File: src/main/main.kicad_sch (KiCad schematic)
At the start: 14 parts, among them J101 Conn_02x05_Odd_Even, P101 SMTSO3035CTJ, P102 SMTSO3035CTJ, P103 SMTSO3035CTJ, P104 SMTSO3035CTJ, U101 LTV-817S

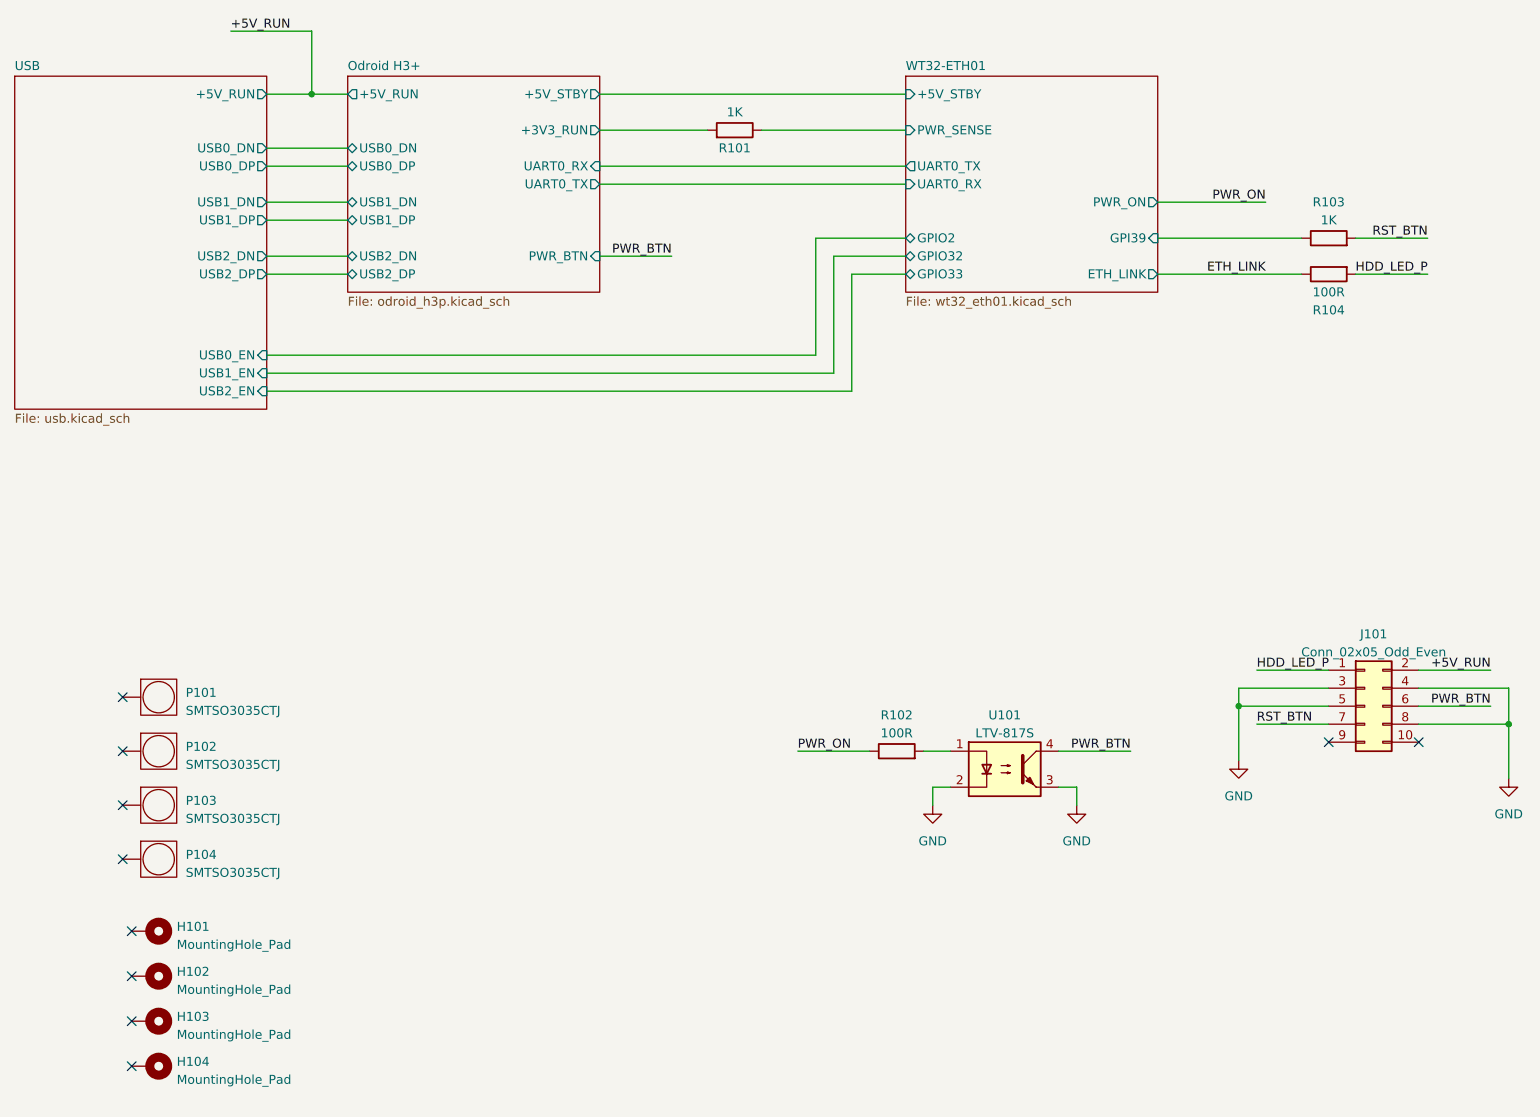
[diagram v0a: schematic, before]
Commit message: Additions and fixes:
Add:
- Add power rail LED status indicators
- Buffered LED on ETH_LINK
- GPIO14 and GPIO12 on header
- GPIO14 5V buffered output on header
- Testpoints for GPIO0 and ESP32_ENABLE pin
- Reset and Boot switches
- ESP PWR selector switch
- USB Type-C PD input (5V) for ESP32
- 1.1A Fuse for USB PD input
- Add spot for BIOS battery on silk
- Add silkscreen default jumper marking
- Add GPIO39 external pullup to 3V3
- Add pulldown to PWR_BUTTON (GPIO15)
- Add silkscreen github link

Fixes:
- Clarify things on silk
- Make pinout compatible with USB-UART boards
  - Move GPI0 and ENABLE to testpoints
- Silkscreen alignment fixes

Removed:
- 3 APA102 LEDs
- Remove JP201
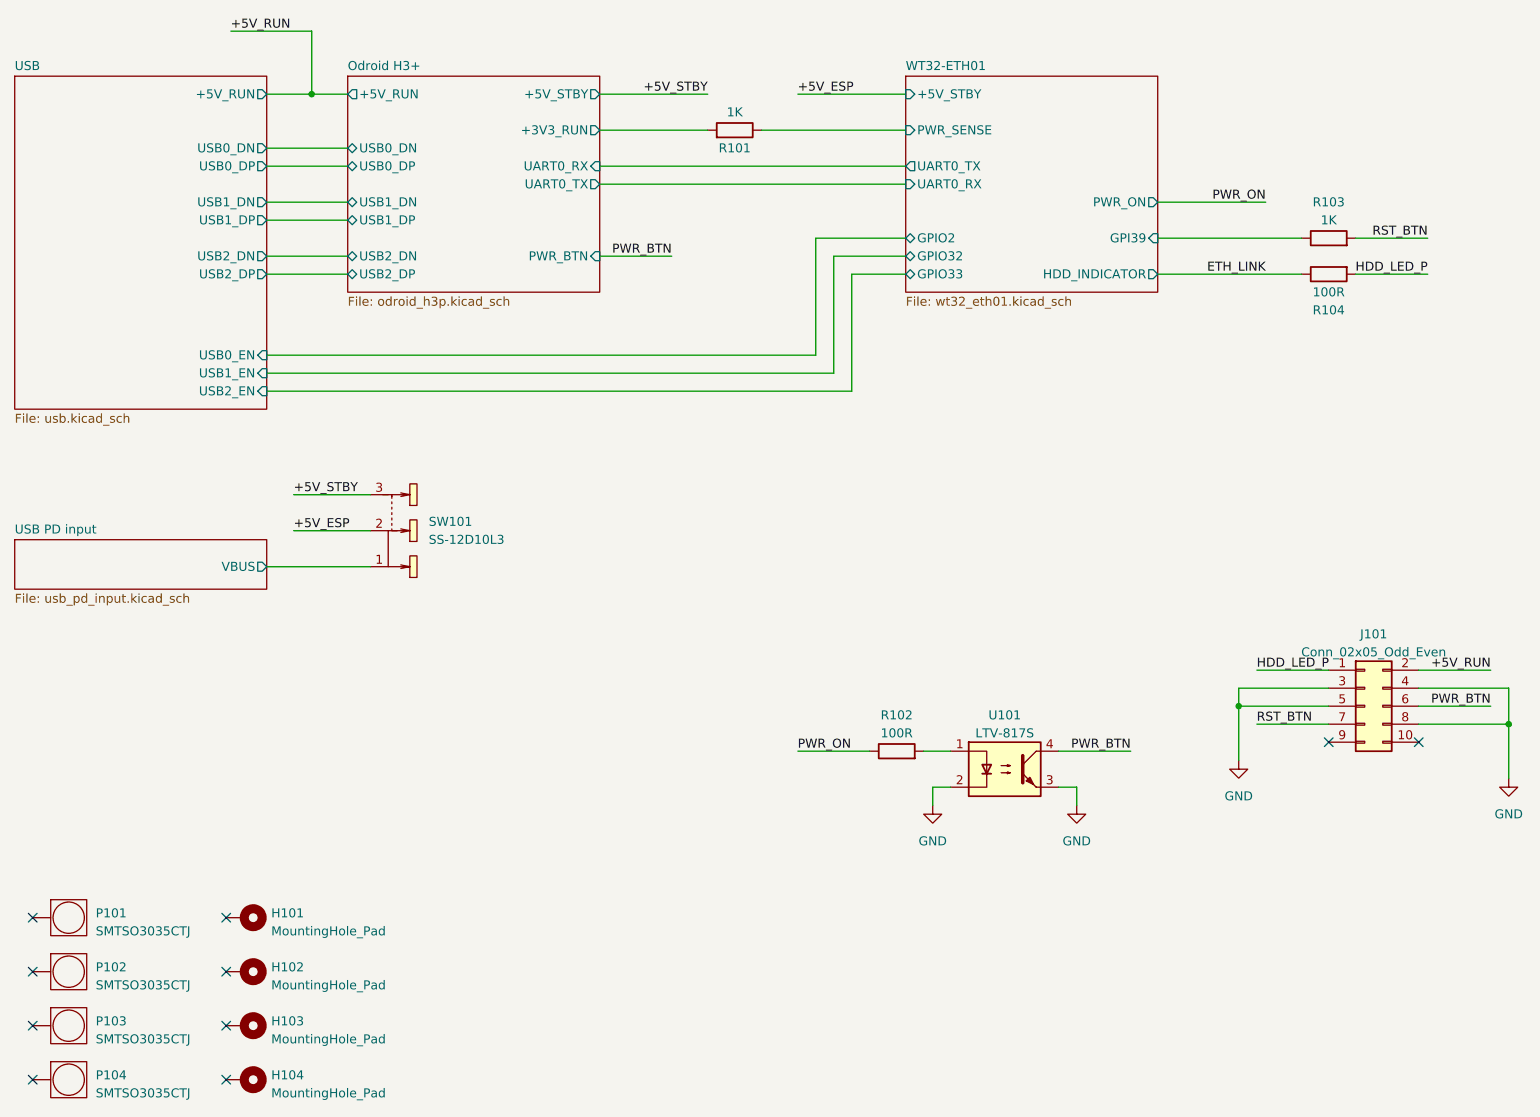
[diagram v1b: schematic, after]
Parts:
- added SW101: SS-12D10L3, easyeda2kicad:SW-TH_SS-12D10L3, symbol easyeda2kicad:SS-12D10L3
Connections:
- new net +5V_ESP: SW101.2
- new net +5V_STBY: SW101.3
- new net USB PD input/VBUS: SW101.1
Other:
- added sheet USB PD input (usb_pd_input.kicad_sch)
- sheet WT32-ETH01 ports: added HDD_INDICATOR; removed ETH_LINK
- moved on the sheet: H101, H102, H103, H104, P101, P102, P103, P104
